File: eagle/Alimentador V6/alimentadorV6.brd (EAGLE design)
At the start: 54.6 x 39.4 mm, 21 parts, among them T1 AO3403, T2 AO3403, T3 AO3403, T4 AO3403

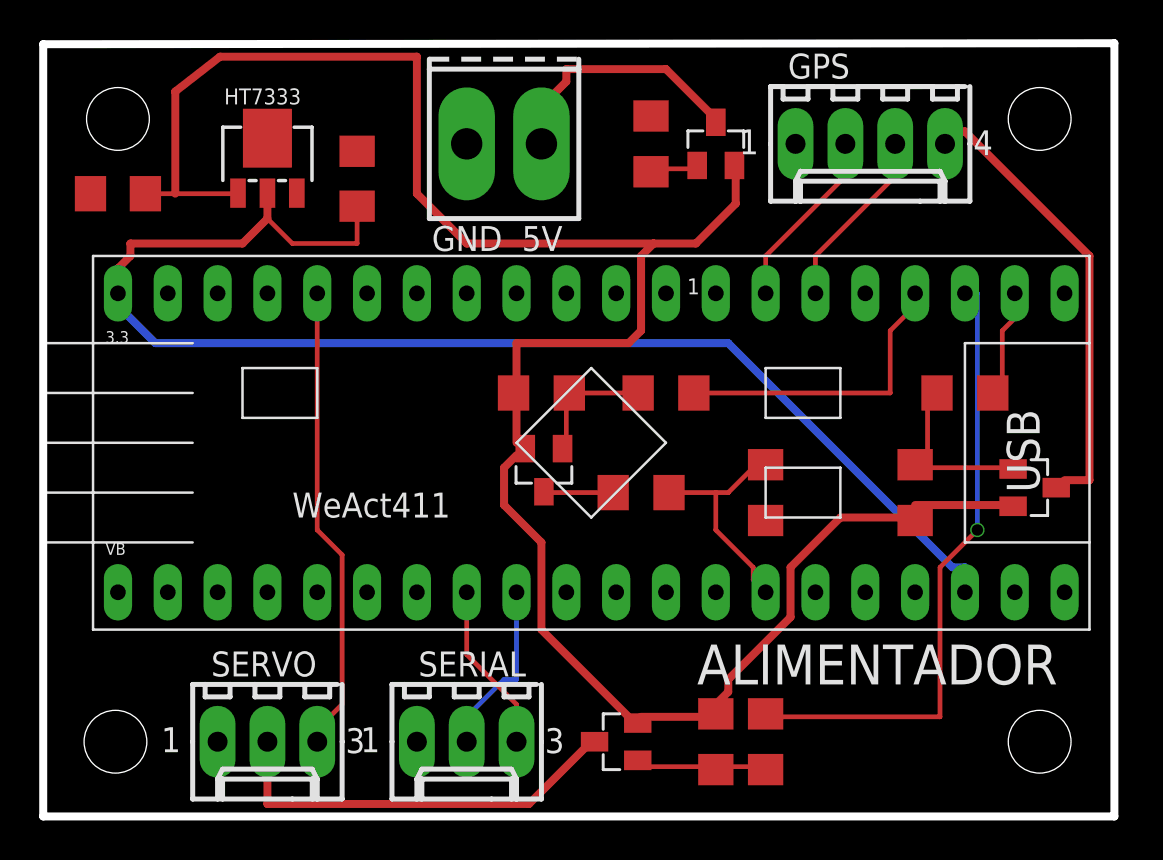
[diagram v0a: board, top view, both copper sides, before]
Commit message: Resuelto misterio consumo
Regulador original era una castaña, con el HT7333 consigo 12 uA en la
placa
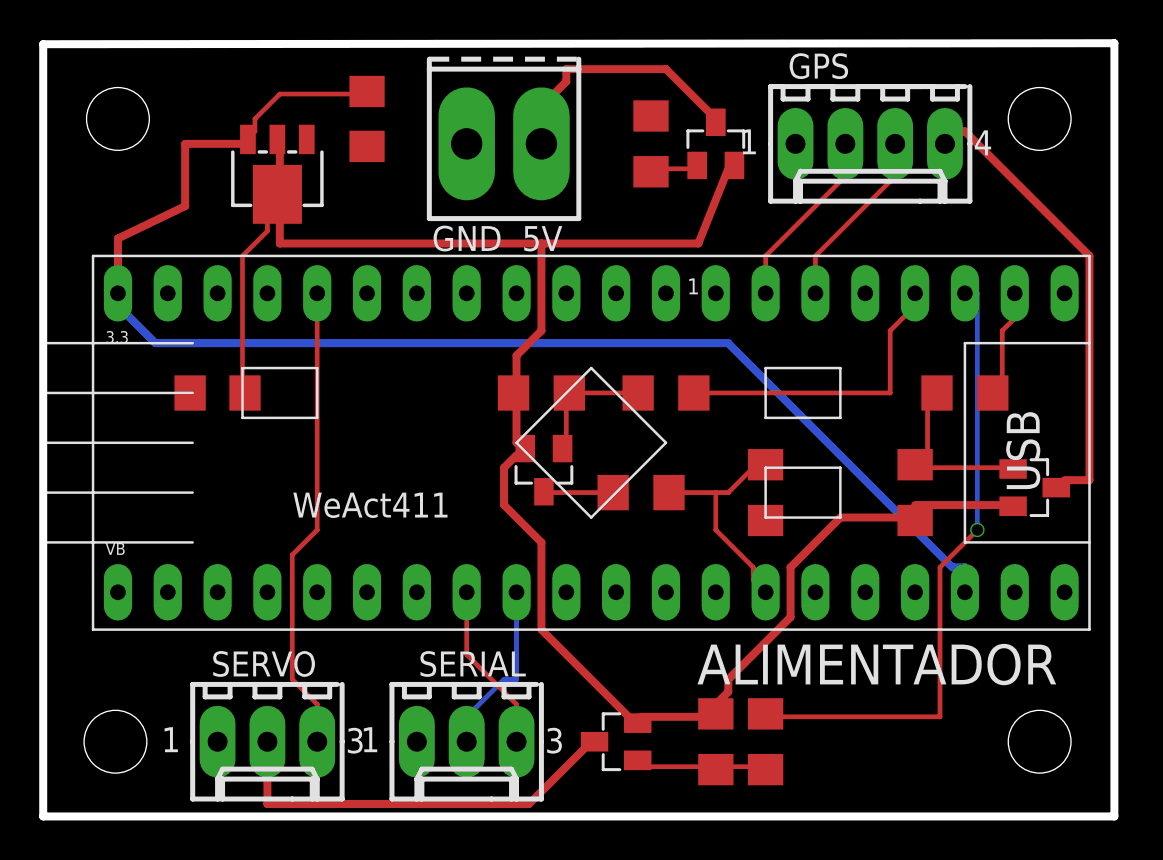
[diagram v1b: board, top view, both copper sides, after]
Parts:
- removed HT7333: HT7133, jcf:SOT89
- added IC1: HT7133, jcf:SOT89
- moved C2 11.4 mm to (7.62, 25.4)
- moved C1 3.09 mm to (15.2, 39.4), turned to 270 degrees
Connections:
- net +3V3: now also IC1.3; no longer HT7333.2
- net +5V: now also IC1.2, IC1.4; no longer HT7333.1
- net GND: now also IC1.1; no longer HT7333.3, HT7333.4
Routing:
- net +5V: track 111.8 -> 97.5 mm
- net +3V3: track 69.2 -> 71.2 mm
- net N$3: track 3.43 -> 2.47 mm
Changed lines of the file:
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@@
 </element>
 <element name="T2" library="jcf" package="SOT23" value="AO3403" x="49.276" y="20.574" smashed="yes" rot="R270">
-<attribute name="VALUE" x="46.228" y="22.098" size="0.8128" layer="27" rot="R270"/>
+<attribute name="VALUE" x="47.244" y="18.034" size="0.8128" layer="27"/>
 </element>
 <element name="R1" library="rcl" package="R1206" value="500k" x="43.18" y="20.32" smashed="yes" rot="R270">
@@
 </element>
 <element name="T1" library="jcf" package="SOT23" value="AO3403" x="24.257" y="21.463" smashed="yes" rot="R180">
-<attribute name="VALUE" x="25.019" y="19.939" size="0.8128" layer="27" rot="R180"/>
+<attribute name="VALUE" x="25.019" y="19.431" size="0.8128" layer="27" rot="R180"/>
 </element>
 <element name="R11" library="rcl" package="R1206" value="500k" x="24.13" y="25.4" smashed="yes" rot="R180">
@@
 <attribute name="NAME" x="23.3411" y="12.2189" size="1.27" layer="25" ratio="10" rot="R180"/>
 </element>
-<element name="HT7333" library="jcf" package="SOT89" value="HT7133" x="10.16" y="37.338" smashed="yes">
-<attribute name="NAME" x="7.955" y="40.1105" size="0.8128" layer="25"/>
-</element>
-<element name="C2" library="rcl" package="C1206" value="10uF" x="2.54" y="35.56" smashed="yes" rot="R180">
-<attribute name="VALUE" x="0.508" y="33.274" size="0.8128" layer="27"/>
-</element>
-<element name="C1" library="rcl" package="C1206" value="10uF" x="14.732" y="36.322" smashed="yes" rot="R90">
-<attribute name="VALUE" x="12.7" y="37.592" size="0.8128" layer="27" rot="R270"/>
+<element name="C2" library="rcl" package="C1206" value="10uF" x="7.62" y="25.4" smashed="yes" rot="R180">
+<attribute name="VALUE" x="5.588" y="23.114" size="0.8128" layer="27"/>
+</element>
+<element name="C1" library="rcl" package="C1206" value="10uF" x="15.24" y="39.37" smashed="yes" rot="R270">
+<attribute name="VALUE" x="17.272" y="38.1" size="0.8128" layer="27" rot="R90"/>
+</element>
+<element name="IC1" library="jcf" package="SOT89" value="HT7133" x="10.668" y="36.576" smashed="yes" rot="R180">
+<attribute name="VALUE" x="12.873" y="40.401" size="0.8128" layer="27" rot="R180"/>
 </element>
 </elements>
@@
 <contactref element="R2" pad="2"/>
 <contactref element="SERIAL" pad="1"/>
-<contactref element="HT7333" pad="3"/>
-<contactref element="HT7333" pad="4"/>
 <contactref element="C2" pad="2"/>
 <contactref element="C1" pad="2"/>
+<contactref element="IC1" pad="1"/>
 </signal>
 <signal name="+5V">
@@
 <contactref element="T1" pad="2"/>
 <contactref element="R11" pad="2"/>
-<contactref element="HT7333" pad="1"/>
 <contactref element="C2" pad="1"/>
+<contactref element="IC1" pad="2"/>
+<contactref element="IC1" pad="4"/>
 <wire x1="33.02" y1="8.89" x2="29.21" y2="8.89" width="0.4064" layer="1"/>
 <wire x1="29.21" y1="8.89" x2="29.04" y2="8.57" width="0.2413" layer="1"/>
@@
 <wire x1="33.02" y1="9.525" x2="33.02" y2="9.042" width="0.2413" layer="1"/>
 <wire x1="43.18" y1="19.05" x2="43.18" y2="18.898" width="0.2413" layer="1"/>
-<wire x1="3.94" y1="35.56" x2="5.461" y2="35.56" width="0.2413" layer="1"/>
-<wire x1="5.461" y1="35.56" x2="8.89" y2="35.56" width="0.2413" layer="1"/>
-<wire x1="8.89" y1="35.56" x2="8.66" y2="35.588" width="0.2413" layer="1"/>
 <wire x1="22.86" y1="25.4" x2="22.86" y2="22.86" width="0.4064" layer="1"/>
-<wire x1="22.86" y1="22.86" x2="23.307" y2="22.563" width="0.2413" layer="1"/>
-<wire x1="29.21" y1="32.385" x2="29.845" y2="33.02" width="0.4064" layer="1"/>
-<wire x1="29.21" y1="28.575" x2="29.21" y2="32.385" width="0.4064" layer="1"/>
-<wire x1="28.575" y1="27.94" x2="29.21" y2="28.575" width="0.4064" layer="1"/>
-<wire x1="22.86" y1="27.94" x2="28.575" y2="27.94" width="0.4064" layer="1"/>
-<wire x1="22.86" y1="25.4" x2="22.86" y2="27.94" width="0.4064" layer="1"/>
+<wire x1="22.86" y1="22.86" x2="23.307" y2="22.563" width="0.4064" layer="1"/>
+<wire x1="32.131" y1="33.02" x2="33.655" y2="36.83" width="0.4064" layer="1"/>
+<wire x1="10.795" y1="33.02" x2="24.13" y2="33.02" width="0.4064" layer="1"/>
+<wire x1="24.13" y1="33.02" x2="32.131" y2="33.02" width="0.4064" layer="1"/>
+<wire x1="10.795" y1="34.925" x2="10.795" y2="33.02" width="0.4064" layer="1"/>
 <wire x1="33.655" y1="36.83" x2="33.97" y2="37" width="0.2413" layer="1"/>
+<wire x1="10.795" y1="34.925" x2="10.668" y2="35.526" width="0.2413" layer="1"/>
+<wire x1="10.795" y1="35.56" x2="10.795" y2="38.1" width="0.4064" layer="1"/>
+<wire x1="10.795" y1="38.1" x2="10.668" y2="38.326" width="0.2413" layer="1"/>
+<wire x1="10.795" y1="35.56" x2="10.668" y2="35.526" width="0.2413" layer="1"/>
+<wire x1="8.89" y1="32.385" x2="8.89" y2="25.4" width="0.2413" layer="1"/>
+<wire x1="10.16" y1="33.655" x2="8.89" y2="32.385" width="0.2413" layer="1"/>
+<wire x1="10.16" y1="34.925" x2="10.16" y2="33.655" width="0.2413" layer="1"/>
+<wire x1="8.89" y1="25.4" x2="9.02" y2="25.4" width="0.2413" layer="1"/>
+<wire x1="10.16" y1="34.925" x2="10.668" y2="35.526" width="0.2413" layer="1"/>
+<wire x1="22.86" y1="27.305" x2="22.86" y2="25.4" width="0.4064" layer="1"/>
+<wire x1="24.13" y1="28.575" x2="22.86" y2="27.305" width="0.4064" layer="1"/>
+<wire x1="24.13" y1="33.02" x2="24.13" y2="28.575" width="0.4064" layer="1"/>
 <wire x1="22.86" y1="25.4" x2="22.708" y2="25.4" width="0.2413" layer="1"/>
-<wire x1="5.461" y1="40.767" x2="5.461" y2="35.56" width="0.4064" layer="1"/>
-<wire x1="7.747" y1="42.545" x2="5.461" y2="40.767" width="0.4064" layer="1"/>
-<wire x1="17.78" y1="42.545" x2="7.747" y2="42.545" width="0.4064" layer="1"/>
-<wire x1="17.78" y1="35.56" x2="17.78" y2="42.545" width="0.4064" layer="1"/>
-<wire x1="20.32" y1="33.02" x2="17.78" y2="35.56" width="0.4064" layer="1"/>
-<wire x1="29.845" y1="33.02" x2="20.32" y2="33.02" width="0.4064" layer="1"/>
 <wire x1="24.13" y1="13.335" x2="28.575" y2="8.89" width="0.4064" layer="1"/>
 <wire x1="24.13" y1="17.78" x2="24.13" y2="13.335" width="0.4064" layer="1"/>
@@
 <wire x1="28.575" y1="8.89" x2="29.04" y2="8.57" width="0.2413" layer="1"/>
 <wire x1="22.86" y1="22.225" x2="23.307" y2="22.563" width="0.2413" layer="1"/>
-<wire x1="29.845" y1="33.02" x2="32.004" y2="33.02" width="0.4064" layer="1"/>
-<wire x1="32.004" y1="33.02" x2="34.036" y2="35.052" width="0.4064" layer="1"/>
-<wire x1="34.036" y1="35.052" x2="34.036" y2="36.934" width="0.4064" layer="1"/>
-<wire x1="34.036" y1="36.934" x2="33.97" y2="37" width="0.4064" layer="1"/>
 </signal>
 <signal name="RST">
@@
 <contactref element="U$2" pad="B8"/>
 <wire x1="12.7" y1="18.415" x2="12.7" y2="30.48" width="0.2413" layer="1"/>
-<wire x1="13.97" y1="17.145" x2="12.7" y2="18.415" width="0.2413" layer="1"/>
-<wire x1="13.97" y1="9.525" x2="13.97" y2="17.145" width="0.2413" layer="1"/>
-<wire x1="12.7" y1="8.255" x2="13.97" y2="9.525" width="0.2413" layer="1"/>
-<wire x1="12.7" y1="7.62" x2="12.7" y2="8.255" width="0.2413" layer="1"/>
+<wire x1="11.43" y1="17.145" x2="12.7" y2="18.415" width="0.2413" layer="1"/>
+<wire x1="11.43" y1="10.795" x2="11.43" y2="17.145" width="0.2413" layer="1"/>
+<wire x1="12.7" y1="9.525" x2="11.43" y2="10.795" width="0.2413" layer="1"/>
+<wire x1="12.7" y1="7.62" x2="12.7" y2="9.525" width="0.2413" layer="1"/>
 </signal>
 <signal name="VCC-GPS">
@@
 <contactref element="R7" pad="1"/>
 <contactref element="T4" pad="1"/>
-<wire x1="29.21" y1="36.83" x2="31.75" y2="36.83" width="0.2413" layer="1"/>
+<wire x1="29.845" y1="36.83" x2="31.75" y2="36.83" width="0.2413" layer="1"/>
 <wire x1="31.75" y1="36.83" x2="32.07" y2="37" width="0.2413" layer="1"/>
-<wire x1="29.21" y1="36.83" x2="29.718" y2="36.678" width="0.2413" layer="1"/>
+<wire x1="29.845" y1="36.83" x2="29.718" y2="36.678" width="0.2413" layer="1"/>
 </signal>
 <signal name="N$2">
@@
 <contactref element="U$2" pad="3V3@1"/>
 <contactref element="U$2" pad="3V3@2"/>
-<contactref element="HT7333" pad="2"/>
 <contactref element="C1" pad="1"/>
-<wire x1="10.16" y1="34.29" x2="10.16" y2="35.588" width="0.4064" layer="1"/>
-<wire x1="11.43" y1="33.02" x2="10.16" y2="34.29" width="0.2413" layer="1"/>
-<wire x1="14.732" y1="33.02" x2="11.43" y2="33.02" width="0.2413" layer="1"/>
-<wire x1="14.732" y1="34.922" x2="14.732" y2="33.02" width="0.2413" layer="1"/>
+<contactref element="IC1" pad="3"/>
+<wire x1="9.525" y1="39.37" x2="9.525" y2="38.735" width="0.2413" layer="1"/>
+<wire x1="10.795" y1="40.64" x2="9.525" y2="39.37" width="0.2413" layer="1"/>
+<wire x1="15.24" y1="40.64" x2="10.795" y2="40.64" width="0.2413" layer="1"/>
+<wire x1="9.525" y1="38.735" x2="9.168" y2="38.326" width="0.2413" layer="1"/>
+<wire x1="15.24" y1="40.64" x2="15.24" y2="40.77" width="0.2413" layer="1"/>
 <wire x1="45.72" y1="16.51" x2="45.72" y2="15.24" width="0.4064" layer="16"/>
 <wire x1="45.085" y1="16.51" x2="45.72" y2="16.51" width="0.4064" layer="16"/>
@@
 <wire x1="2.54" y1="29.845" x2="4.445" y2="27.94" width="0.4064" layer="16"/>
 <wire x1="2.54" y1="30.48" x2="2.54" y2="29.845" width="0.4064" layer="16"/>
-<wire x1="8.89" y1="33.02" x2="10.16" y2="34.29" width="0.4064" layer="1"/>
-<wire x1="3.175" y1="33.02" x2="8.89" y2="33.02" width="0.4064" layer="1"/>
-<wire x1="3.175" y1="32.385" x2="3.175" y2="33.02" width="0.4064" layer="1"/>
-<wire x1="2.54" y1="31.75" x2="3.175" y2="32.385" width="0.4064" layer="1"/>
-<wire x1="2.54" y1="30.48" x2="2.54" y2="31.75" width="0.4064" layer="1"/>
+<wire x1="5.969" y1="38.1" x2="8.89" y2="38.1" width="0.4064" layer="1"/>
+<wire x1="5.969" y1="34.925" x2="5.969" y2="38.1" width="0.4064" layer="1"/>
+<wire x1="2.54" y1="33.274" x2="5.969" y2="34.925" width="0.4064" layer="1"/>
+<wire x1="2.54" y1="30.48" x2="2.54" y2="33.274" width="0.4064" layer="1"/>
+<wire x1="8.89" y1="38.1" x2="9.168" y2="38.326" width="0.2413" layer="1"/>
 </signal>
 </signals>
